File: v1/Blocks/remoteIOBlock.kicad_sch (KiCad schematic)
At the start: 1 part, among them IC44 PCA9555PW,118

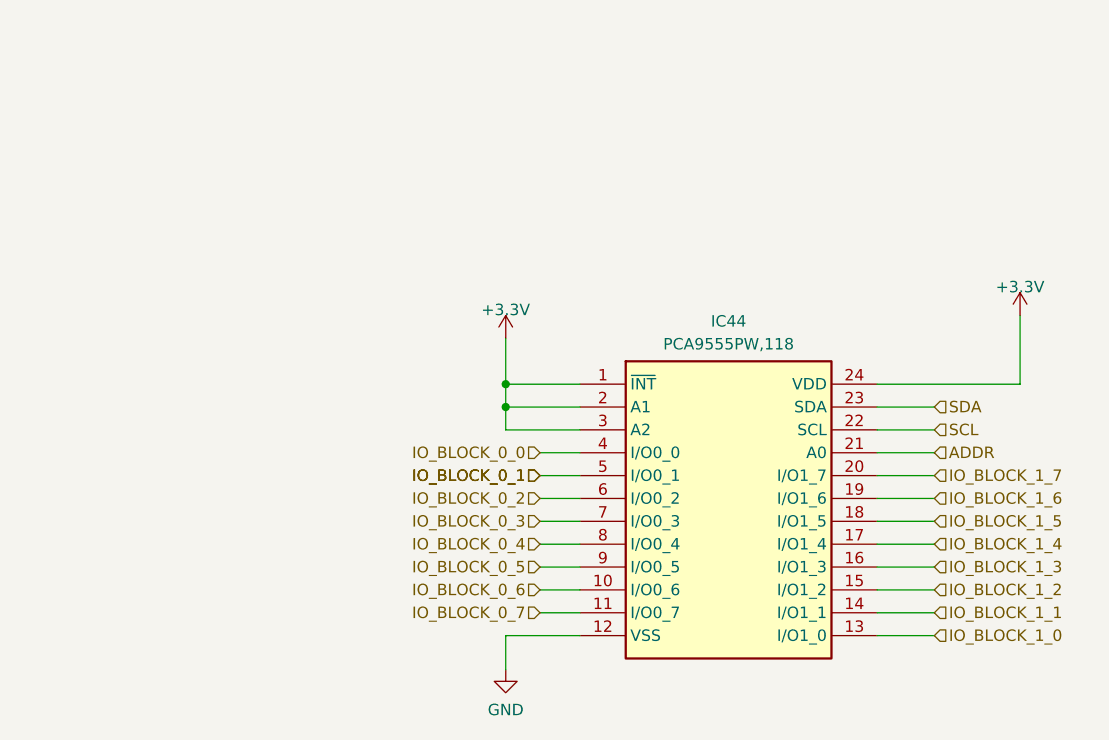
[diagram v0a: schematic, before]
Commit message: Update views, to make drawing sheets smaller where necessary
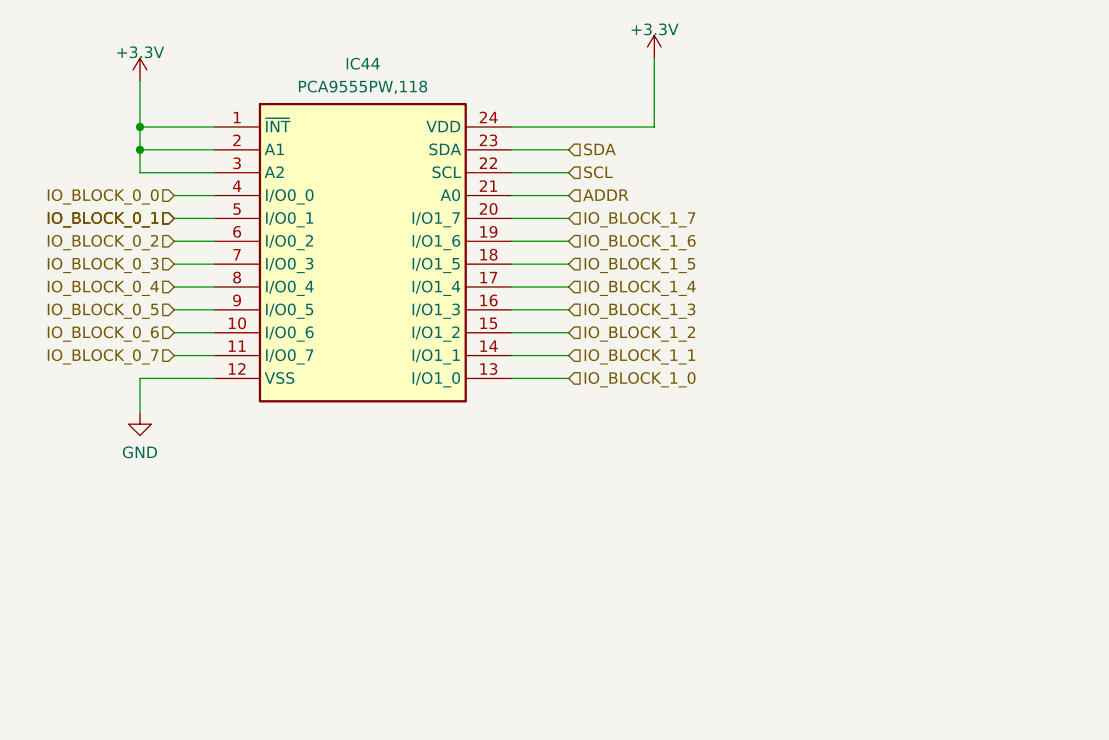
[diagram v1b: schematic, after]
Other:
- moved on the sheet: IC44
